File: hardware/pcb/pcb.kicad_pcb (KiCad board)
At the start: 2 copper layers, 4 parts, among them J1 L_GPIO, J2 R_GPIO, U1 ESP32-C3-WROOM-02

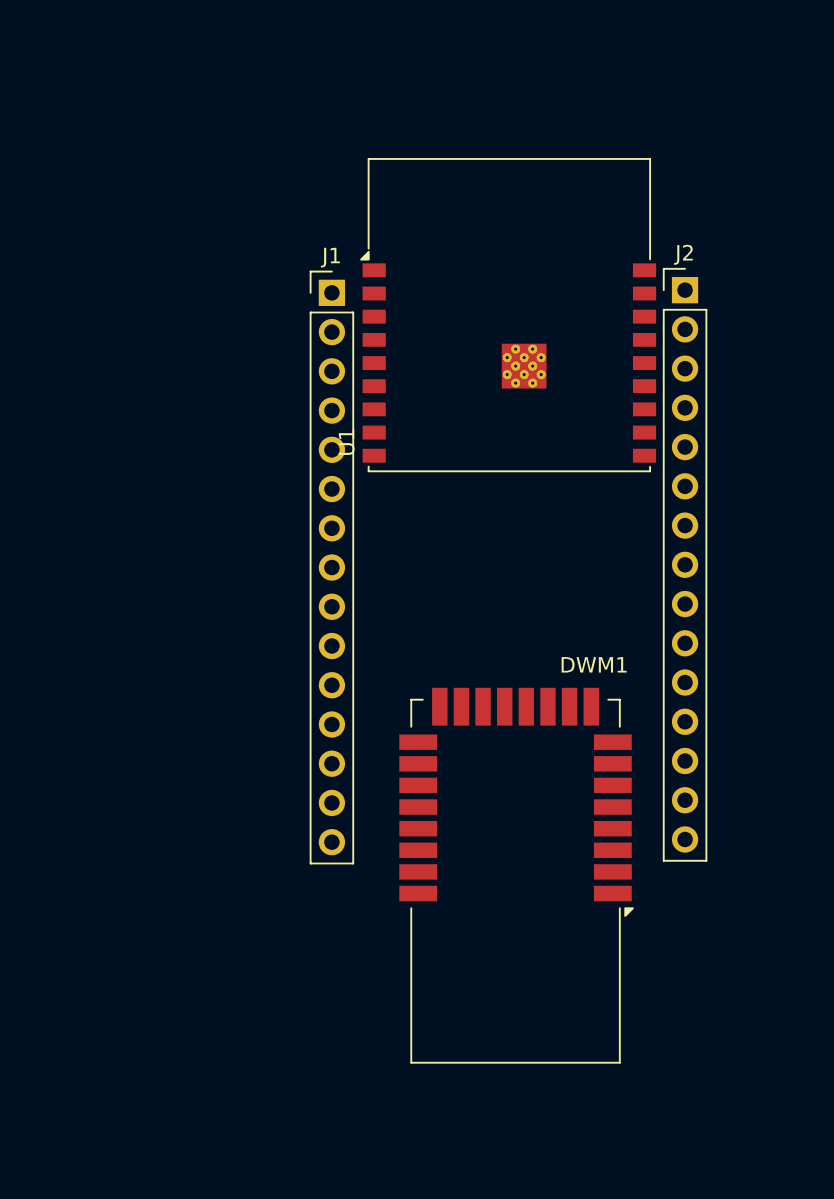
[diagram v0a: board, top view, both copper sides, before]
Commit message: PCB: progress on schematic
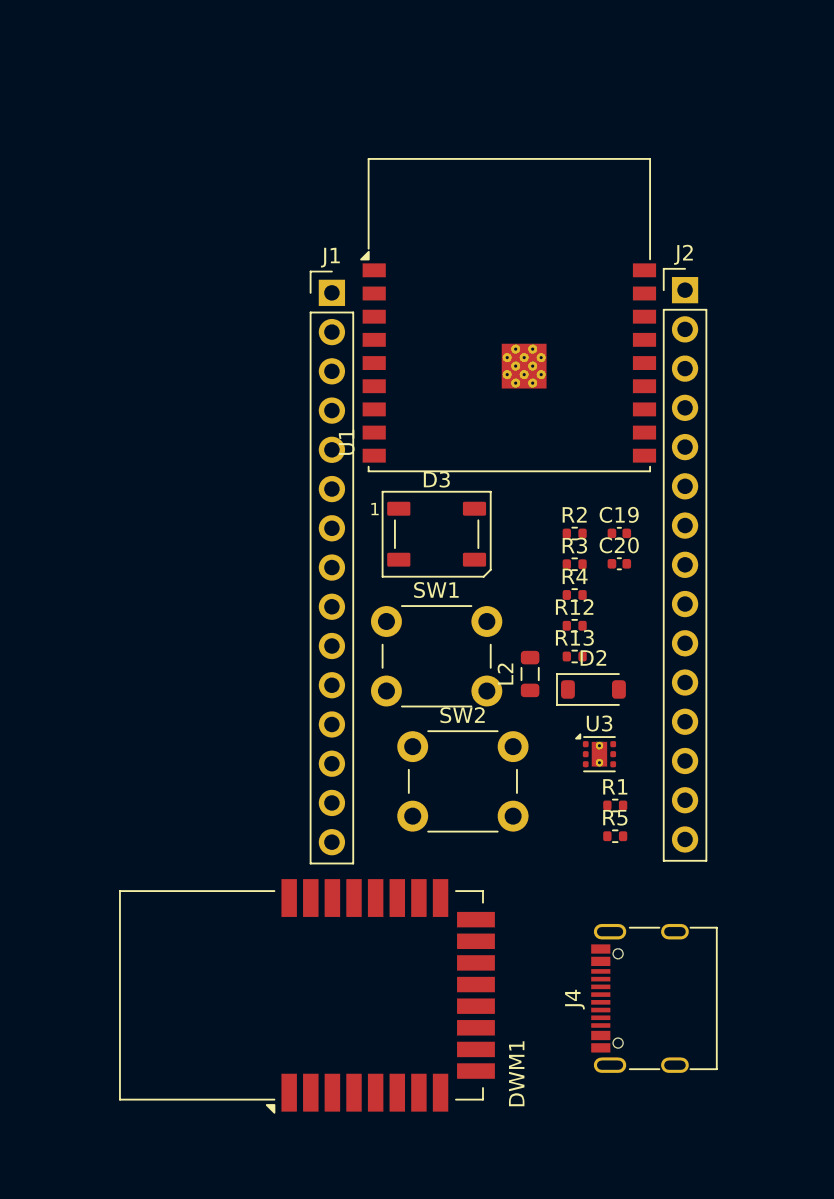
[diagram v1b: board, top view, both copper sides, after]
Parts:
- added C19: 10uF, Capacitor_SMD:C_0402_1005Metric, F.Cu at (110.0, 67.4)
- added C20: 10uF, Capacitor_SMD:C_0402_1005Metric, F.Cu at (110.0, 69.4)
- added D2: D_shottky, Diode_SMD:D_SOD-123, F.Cu at (108.4, 77.5)
- added D3: WS2812B, LED_SMD:LED_WS2812B_PLCC4_5.0x5.0mm_P3.2mm, F.Cu at (98.2, 67.4)
- added J4: USB_C_Receptacle_USB2.0_14P, Connector_USB:USB_C_Receptacle_G-Switch_GT-USB-7010ASV, F.Cu at (112.6, 97.5)
- added L2: 2.2uH 1.2A, Inductor_SMD:L_0805_2012Metric, F.Cu at (104.3, 76.5)
- added R1: 10k, Resistor_SMD:R_0402_1005Metric, F.Cu at (109.8, 85.0)
- added R12: 5.1k, Resistor_SMD:R_0402_1005Metric, F.Cu at (107.2, 73.4)
- added R13: 5.1k, Resistor_SMD:R_0402_1005Metric, F.Cu at (107.2, 75.4)
- added R2: 10k, Resistor_SMD:R_0402_1005Metric, F.Cu at (107.2, 67.4)
- added R3: 10k, Resistor_SMD:R_0402_1005Metric, F.Cu at (107.2, 69.4)
- added R4: 10k, Resistor_SMD:R_0402_1005Metric, F.Cu at (107.2, 71.4)
- added R5: 10k, Resistor_SMD:R_0402_1005Metric, F.Cu at (109.8, 87.0)
- added SW1: SW_Push, Button_Switch_THT:SW_PUSH_6mm, F.Cu at (95.0, 73.1)
- added SW2: SW_Push, Button_Switch_THT:SW_PUSH_6mm, F.Cu at (96.7, 81.2)
- added U3: TPS62291, Package_SON:WSON-6-1EP_2x2mm_P0.65mm_EP1x1.6mm_ThermalVias, F.Cu at (108.8, 81.7)
- moved DWM1 15.7 mm to (89.5, 97.3), turned to 90 degrees
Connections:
- U1 pad 10: unconnected-(U1-IO10-Pad10) -> /U-RSTn
- U1 pad 13: unconnected-(U1-IO18-Pad13) -> USB_D-
- U1 pad 14: unconnected-(U1-IO19-Pad14) -> USB_D+
- U1 pad 15: unconnected-(U1-IO3-Pad15) -> /U-IRQ
- U1 pad 16: unconnected-(U1-IO2-Pad16) -> Net-(U1-IO2)
- U1 pad 17: unconnected-(U1-IO1-Pad17) -> /LED
- U1 pad 18: unconnected-(U1-IO0-Pad18) -> /BUTTON
- U1 pad 2: unconnected-(U1-EN-Pad2) -> /ENABLE
- U1 pad 7: /U-IRQ -> Net-(U1-IO8)
- U1 pad 8: /U-RSTn -> Net-(U1-IO9)

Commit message: finished schematic and routed pcb
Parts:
- added D1: TXLED, LED_SMD:LED_0402_1005Metric, F.Cu at (104.6, 83.0)
- added D4: RXLED, LED_SMD:LED_0402_1005Metric, F.Cu at (102.3, 83.0)
- added D5: SFDLED, LED_SMD:LED_0402_1005Metric, F.Cu at (100.0, 83.0)
- added D6: RXOKLED, LED_SMD:LED_0402_1005Metric, F.Cu at (97.8, 83.0)
- added R6: R_Small, Resistor_SMD:R_0402_1005Metric, F.Cu at (104.6, 85.8)
- added R7: R_Small, Resistor_SMD:R_0402_1005Metric, F.Cu at (102.3, 85.8)
- added R8: R_Small, Resistor_SMD:R_0402_1005Metric, F.Cu at (100.0, 85.8)
- added R9: R_Small, Resistor_SMD:R_0402_1005Metric, F.Cu at (97.8, 85.7)
- SW1: value SW_Push -> MODE
- SW2: value SW_Push -> RESET
- moved R5 23.5 mm to (95.6, 68.3), turned to -90 degrees
- moved R12 22.1 mm to (107.1, 95.5)
- moved D2 21.4 mm to (107.1, 98.9), turned to 90 degrees
- moved C19 18.7 mm to (111.0, 86.1), turned to -90 degrees
- moved R13 17.7 mm to (107.1, 93.0)
- moved C20 16.7 mm to (109.2, 86.0), turned to -90 degrees
- moved R1 14.8 mm to (95.0, 85.6), turned to 90 degrees
- moved SW1 12.3 mm to (106.2, 78.1), turned to 90 degrees
- moved R2 11.8 mm to (95.6, 65.3), turned to 90 degrees
- moved D3 10.4 mm to (108.5, 66.7)
- moved SW2 9.99 mm to (99.6, 71.6), turned to -90 degrees
- moved R3 8.36 mm to (99.9, 65.3), turned to 90 degrees
- moved R4 7.89 mm to (99.9, 68.3), turned to 90 degrees
- moved L2 7.11 mm to (107.4, 82.9)
- moved USB-C 2.81 mm to (113.4, 94.8)
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- renumbered J4 to USB-C
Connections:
- DWM1 pad 12: unconnected-(DWM1-GPIO3/TXLED-Pad12) -> /TXLED
- DWM1 pad 13: unconnected-(DWM1-GPIO2/RXLED-Pad13) -> /RXLED
- DWM1 pad 14: unconnected-(DWM1-GPIO1/SFDLED-Pad14) -> /SFDLED
- DWM1 pad 15: unconnected-(DWM1-GPIO0/RXOKLED-Pad15) -> /RXOKLED
- J1 pad 3: VUSB -> +5V
- U1 pad 11: unconnected-(U1-IO20/RXD-Pad11) -> /RXD
- U1 pad 12: unconnected-(U1-IO21/TXD-Pad12) -> /TXD
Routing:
- net +3V3: track 0.00 -> 121.5 mm, vias 0 -> 4
- net +5V: track 0.00 -> 75.2 mm, vias 0 -> 2
- net /U-RSTn: track 0.00 -> 62.1 mm
- net USB_D-: track 0.00 -> 54.4 mm, vias 0 -> 2
- net USB_D+: track 0.00 -> 53.1 mm, vias 0 -> 2
- net /U-IRQ: track 0.00 -> 48.3 mm
- net /U-SPIMISO: track 0.00 -> 48.2 mm, vias 0 -> 2
- net /U-SPIMOSI: track 0.00 -> 43.6 mm, vias 0 -> 2
- net /U-SPICLK: track 0.00 -> 40.4 mm, vias 0 -> 2
- net /U-SPICSn: track 0.00 -> 36.3 mm, vias 0 -> 2
- net /ENABLE: track 0.00 -> 30.4 mm, vias 0 -> 1
- net /BUTTON: track 0.00 -> 29.0 mm, vias 0 -> 1
- net /TXD: track 0.00 -> 26.8 mm, vias 0 -> 1
- net Net-(U1-IO2): track 0.00 -> 23.0 mm
- net /RXD: track 0.00 -> 22.1 mm, vias 0 -> 1
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- added copper zone on B.Cu, net GND
- added copper zone on F.Cu, net GND
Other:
- board outline added: 26.7 x 56.6 mm

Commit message: PCB progress
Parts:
- renumbered SW1 to MODE, SW2 to RESET, D4 to RXLED, D6 to RXOKLED, D5 to SFDLED, D1 to TXLED
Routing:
- net GND: track 15.5 -> 16.9 mm
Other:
- outline, holes or cut-outs redrawn
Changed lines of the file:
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@@
 		(descr "LED SMD 0402 (1005 Metric), square (rectangular) end terminal, IPC-7351 nominal, (Body size source: http://www.tortai-tech.com/upload/download/2011102023233369053.pdf), generated with kicad-footprint-generator")
 		(tags "LED")
-		(property "Reference" "D5"
+		(property "Reference" "SFDLED"
 			(at 0 -1.17 90)
 			(layer "F.SilkS")
@@
 		(descr "LED SMD 0402 (1005 Metric), square (rectangular) end terminal, IPC-7351 nominal, (Body size source: http://www.tortai-tech.com/upload/download/2011102023233369053.pdf), generated with kicad-footprint-generator")
 		(tags "LED")
-		(property "Reference" "D6"
+		(property "Reference" "RXOKLED"
 			(at 0 -1.17 90)
 			(layer "F.SilkS")
@@
 		(tags "resistor")
 		(property "Reference" "R8"
-			(at 0 -1.17 90)
+			(at 2.034 -0.032 90)
 			(layer "F.SilkS")
 			(effects
@@
 		(descr "Generic 6mm SW tactile push button")
 		(tags "tact sw push 6mm")
-		(property "Reference" "SW1"
+		(property "Reference" "MODE"
 			(at 3.25 -2 90)
 			(layer "F.SilkS")
@@
 		(descr "LED SMD 0402 (1005 Metric), square (rectangular) end terminal, IPC-7351 nominal, (Body size source: http://www.tortai-tech.com/upload/download/2011102023233369053.pdf), generated with kicad-footprint-generator")
 		(tags "LED")
-		(property "Reference" "D1"
+		(property "Reference" "TXLED"
 			(at 0 -1.17 90)
 			(layer "F.SilkS")
@@
 		(tags "resistor")
 		(property "Reference" "R9"
-			(at 0 -1.17 90)
+			(at 2.158 -0.032 90)
 			(layer "F.SilkS")
 			(effects
@@
 		(tags "resistor")
 		(property "Reference" "R6"
-			(at 0 -1.17 90)
+			(at 2.034 0 90)
 			(layer "F.SilkS")
 			(effects
@@
 		(descr "Generic 6mm SW tactile push button")
 		(tags "tact sw push 6mm")
-		(property "Reference" "SW2"
+		(property "Reference" "RESET"
 			(at 3.25 -2 90)
 			(layer "F.SilkS")
@@
 		(descr "LED SMD 0402 (1005 Metric), square (rectangular) end terminal, IPC-7351 nominal, (Body size source: http://www.tortai-tech.com/upload/download/2011102023233369053.pdf), generated with kicad-footprint-generator")
 		(tags "LED")
-		(property "Reference" "D4"
+		(property "Reference" "RXLED"
 			(at 0 -1.17 90)
 			(layer "F.SilkS")
@@
 		(tags "resistor")
 		(property "Reference" "R7"
-			(at 0 -1.17 90)
+			(at 2.034 -0.032 90)
 			(layer "F.SilkS")
 			(effects
@@
 		)
 	)
-	(gr_rect
-		(start 89.3652 49.1)
-		(end 116.078 105.7402)
+	(gr_line
+		(start 116.078 51.1)
+		(end 116.078 103.7402)
+		(stroke
+			(width 0.05)
+			(type default)
+		)
+		(layer "Edge.Cuts")
+	)
+	(gr_arc
+		(start 91.3652 105.7402)
+		(mid 89.950986 105.154414)
+		(end 89.3652 103.7402)
+		(stroke
+			(width 0.05)
+			(type default)
+		)
+		(layer "Edge.Cuts")
+	)
+	(gr_line
+		(start 114.078 105.7402)
+		(end 91.3652 105.7402)
+		(stroke
+			(width 0.05)
+			(type default)
+		)
+		(layer "Edge.Cuts")
+	)
+	(gr_arc
+		(start 116.078 103.7402)
+		(mid 115.492214 105.154414)
+		(end 114.078 105.7402)
+		(stroke
+			(width 0.05)
+			(type default)
+		)
+		(layer "Edge.Cuts")
+	)
+	(gr_line
+		(start 89.3652 103.7402)
+		(end 89.3652 51.1)
+		(stroke
+			(width 0.05)
+			(type default)
+		)
+		(layer "Edge.Cuts")
+	)
+	(gr_line
+		(start 91.3652 49.1)
+		(end 114.078 49.1)
+		(stroke
+			(width 0.05)
+			(type default)
+		)
+		(layer "Edge.Cuts")
+	)
+	(gr_arc
+		(start 89.3652 51.1)
+		(mid 89.950986 49.685786)
+		(end 91.3652 49.1)
+		(stroke
+			(width 0.05)
+			(type default)
+		)
+		(layer "Edge.Cuts")
+	)
+	(gr_arc
+		(start 114.078 49.1)
+		(mid 115.492214 49.685786)
+		(end 116.078 51.1)
 		(stroke
 			(width 0.05)
 			(type default)
 		)
-		(fill no)
 		(layer "Edge.Cuts")
 	)
@@
 	)
 	(segment
+		(start 109.7112 91.0982)
+		(end 110.3112 90.4982)
+		(width 0.2)
+		(layer "F.Cu")
+		(net 1)
+	)
+	(segment
+		(start 109.7112 91.6182)
+		(end 109.7112 91.0982)
+		(width 0.2)
+		(layer "F.Cu")
+		(net 1)
+	)
+	(segment

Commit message: PCB progress
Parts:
- moved C20 0.10 mm to (109.2, 86.1)
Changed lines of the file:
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@@
 	(footprint "Capacitor_SMD:C_0402_1005Metric"
 		(layer "F.Cu")
-		(at 109.22 86.003 -90)
+		(at 109.22 86.106 -90)
 		(descr "Capacitor SMD 0402 (1005 Metric), square (rectangular) end terminal, IPC-7351 nominal, (Body size source: IPC-SM-782 page 76, https://www.pcb-3d.com/wordpress/wp-content/uploads/ipc-sm-782a_amendment_1_and_2.pdf), generated with kicad-footprint-generator")
 		(tags "capacitor")
@@
 	)
 	(segment
-		(start 109.22 85.523)
-		(end 109.22 84.1635)
-		(width 0.4)
-		(layer "F.Cu")
-		(net 4)
-	)
-	(segment
 		(start 107.4674 84.6346)
 		(end 107.4674 83.9135)
@@
 		(width 0.4)
 		(layer "F.Cu")
+		(net 4)
+	)
+	(segment
+		(start 109.22 85.626)
+		(end 109.22 84.1635)
+		(width 0.4)
+		(layer "F.Cu")

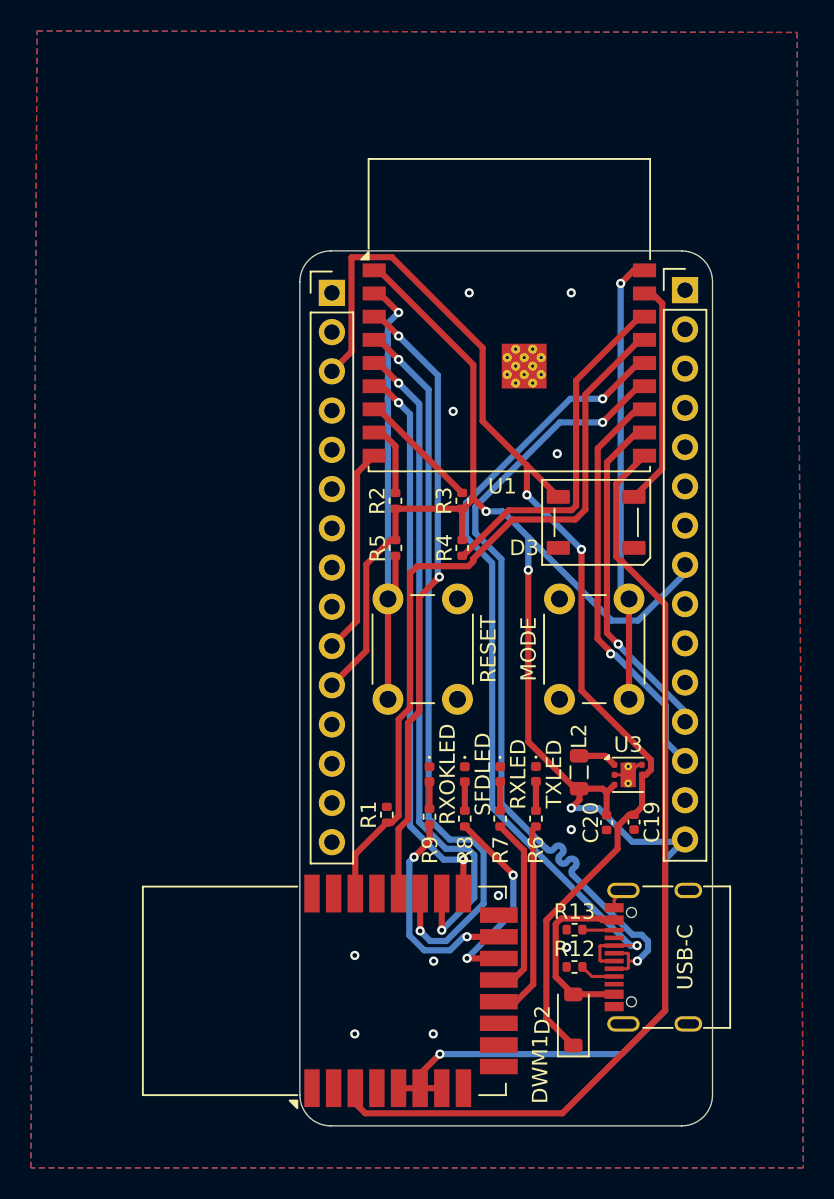
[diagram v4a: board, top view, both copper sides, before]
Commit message: added LCSC parts ids for assembly
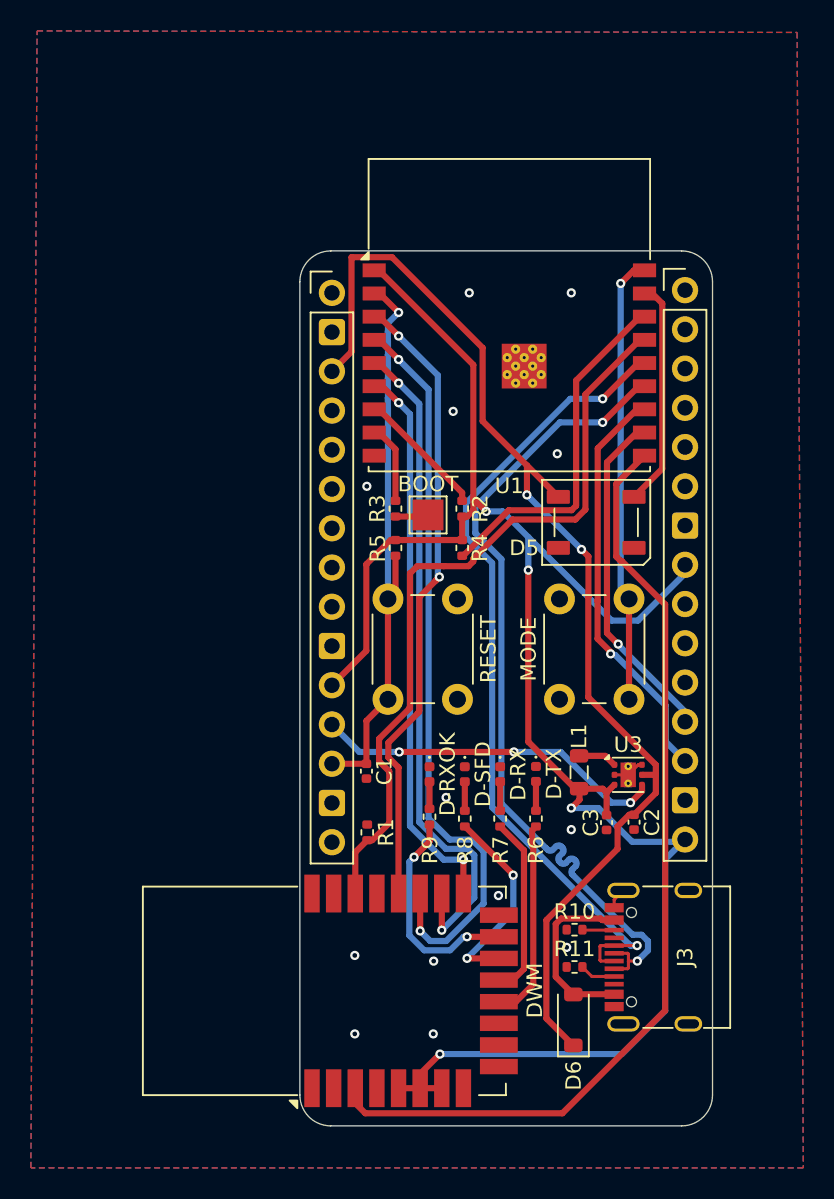
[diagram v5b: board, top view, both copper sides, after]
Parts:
- added BOOT: TestPoint, TestPoint:TestPoint_Pad_2.0x2.0mm, F.Cu at (97.7, 66.2)
- added C1: 100nf, Capacitor_SMD:C_0402_1005Metric, F.Cu at (93.7, 82.8)
- moved R3 4.35 mm to (95.6, 65.8)
- moved R2 4.35 mm to (99.9, 65.8), turned to -90 degrees
- moved R1 1.71 mm to (93.7, 86.7)
- renumbered C19 to C2, C20 to C3, RXLED to D-RX, RXOKLED to D-RXOK, SFDLED to D-SFD, TXLED to D-TX, D3 to D5, D2 to D6, DWM1 to DWM, USB-C to J3, L2 to L1, R13 to R10, R12 to R11
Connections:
- J1 pad 12: /EN -> /SD-EN
- J1 pad 13: /RST -> /ENABLE
- R2 pad 1: +3V3 -> Net-(U1-IO8)
- R2 pad 2: Net-(U1-IO9) -> +3V3
- R3 pad 1: +3V3 -> Net-(R3-Pad1)
- R3 pad 2: Net-(U1-IO8) -> Net-(U1-IO9)
- U3 pad 4: +5V -> /SD-EN
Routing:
- net /SD-EN: track 0.00 -> 22.9 mm, vias 0 -> 3
- net GND: track 16.9 -> 3.41 mm, vias 11 -> 13
- net /ENABLE: track 30.4 -> 38.0 mm
- net Net-(R3-Pad1): track 0.00 -> 2.15 mm
- net +3V3: track 121.6 -> 119.7 mm
- net +5V: track 75.2 -> 76.3 mm
- net Net-(U1-IO9): track 4.78 -> 5.67 mm
- net /U-IRQ: track 48.3 -> 48.8 mm
- net /U-SPICLK: track 40.4 -> 40.9 mm
- net Net-(U1-IO8): track 7.94 -> 8.45 mm
